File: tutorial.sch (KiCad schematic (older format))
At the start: 129 parts, among them SW0:0 CTRL, SW0:1 SUPER, SW0:10 ALT, SW0:11 MENU, SW0:12 SUPER, SW0:13 CTRL, SW0:2 ALT, SW0:7 SPACE, SW1:0 SHIFT, SW1:10 ., SW1:11 ?, SW1:13 SHIFT, SW1:2 Z, SW1:3 X, SW1:4 C, SW1:5 V, SW1:6 B, SW1:7 N, SW1:8 M, SW1:9 ,, SW2:0 CAPS, SW2:1 A, SW2:10 ;, SW2:11 ', SW2:13 ENTER, SW2:2 S, SW2:3 D, SW2:4 F, SW2:5 G, SW2:6 H, SW2:7 J, SW2:8 K, SW2:9 L, SW3:0 TAB, SW3:1 Q, SW3:10 P, SW3:11 {, SW3:12 }, SW3:13 BCKSL, SW3:2 W, SW3:3 E, SW3:4 R, SW3:5 T, SW3:6 Y, SW3:7 U, SW3:8 I, SW3:9 O, SW4:0 TILDE, SW4:1 1, SW4:10 0, SW4:11 -, SW4:12 =, SW4:13 BCKSP, SW4:2 2, SW4:3 3, SW4:4 4, SW4:5 5, SW4:6 6, SW4:7 7, SW4:8 8, SW4:9 9, U1 TEENSY2.0

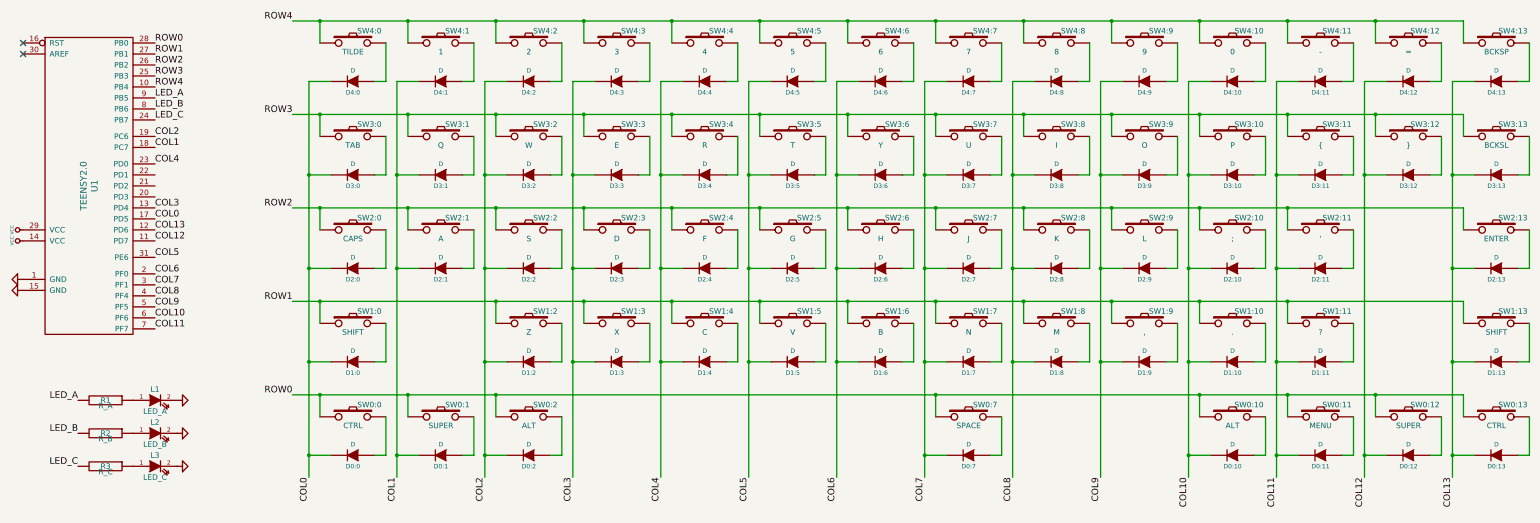
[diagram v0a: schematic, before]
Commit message: Updated to "new" KiCAD formats
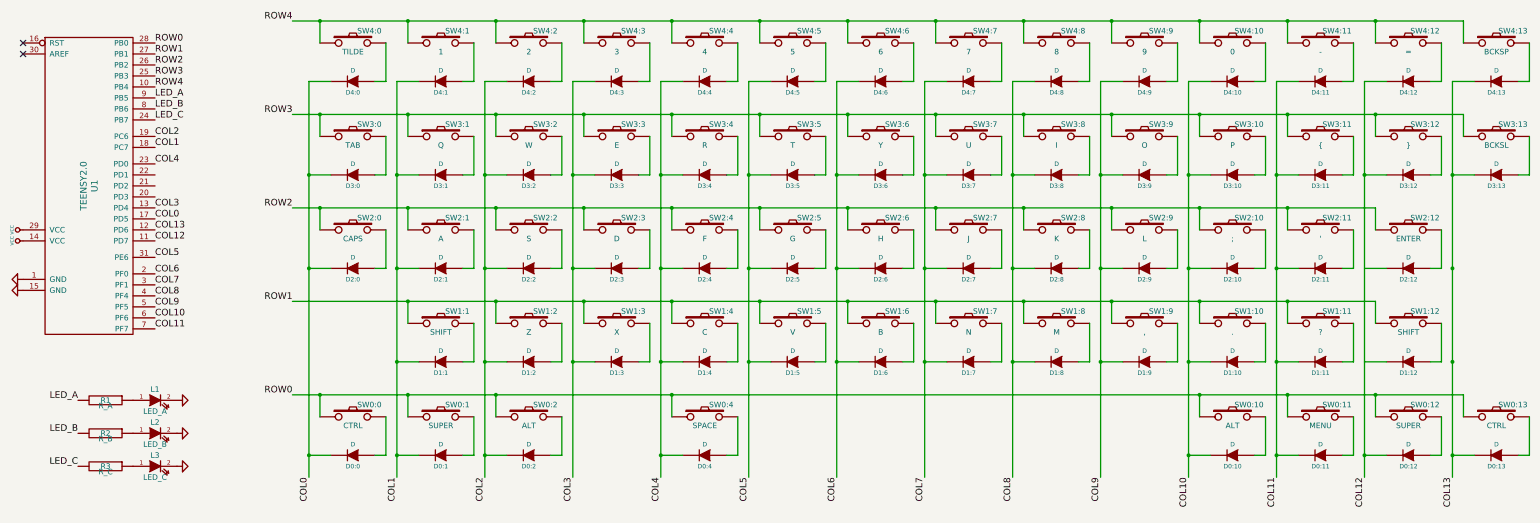
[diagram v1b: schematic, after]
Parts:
- D0:0, D0:1, D0:10, D0:11, D0:12, D0:13, D0:2, D1:10, D1:11, D1:2, D1:3, D1:4, D1:5, D1:6, D1:7, D1:8, D1:9, D2:0, D2:1, D2:10, D2:11, D2:2, D2:3, D2:4, D2:5, D2:6, D2:7, D2:8, D2:9, D3:0, D3:1, D3:10, D3:11, D3:12, D3:13, D3:2, D3:3, D3:4, D3:5, D3:6, D3:7, D3:8, D3:9, D4:0, D4:1, D4:10, D4:11, D4:12, D4:13, D4:2, D4:3, D4:4, D4:5, D4:6, D4:7, D4:8, D4:9: footprint (none) -> footprints:DIODE
- D0:4: renamed from D0:7; footprint (none) -> footprints:DIODE
- D1:1: renamed from D1:0; footprint (none) -> footprints:DIODE
- D1:12: renamed from D1:13; footprint (none) -> footprints:DIODE
- D2:12: renamed from D2:13; footprint (none) -> footprints:DIODE
- L1, L2, L3: footprint (none) -> footprints:CHERRY_MX_LED
- R1, R2, R3: footprint (none) -> footprints:RESISTOR
- SW0:0, SW0:1, SW0:10, SW0:11, SW0:12, SW0:13, SW0:2: footprint (none) -> footprints:CHERRY_PCB_125H
- SW0:4: renamed from SW0:7; footprint (none) -> footprints:CHERRY_PCB_625H
- SW1:1: renamed from SW1:0; footprint (none) -> footprints:CHERRY_PCB_225H
- SW1:10, SW1:11, SW1:2, SW1:3, SW1:4, SW1:5, SW1:6, SW1:7, SW1:8, SW1:9, SW2:1, SW2:10, SW2:11, SW2:2, SW2:3, SW2:4, SW2:5, SW2:6, SW2:7, SW2:8, SW2:9, SW3:1, SW3:10, SW3:11, SW3:12, SW3:2, SW3:3, SW3:4, SW3:5, SW3:6, SW3:7, SW3:8, SW3:9, SW4:0, SW4:1, SW4:10, SW4:11, SW4:12, SW4:2, SW4:3, SW4:4, SW4:5, SW4:6, SW4:7, SW4:8, SW4:9: footprint (none) -> footprints:CHERRY_PCB_100H
- SW1:12: renamed from SW1:13; footprint (none) -> footprints:CHERRY_PCB_275H
- SW2:0: footprint (none) -> footprints:CHERRY_PCB_175H
- SW2:12: renamed from SW2:13; footprint (none) -> footprints:CHERRY_PCB_225H
- SW3:0, SW3:13: footprint (none) -> footprints:CHERRY_PCB_150H
- SW4:13: footprint (none) -> footprints:CHERRY_PCB_200H
- U1: footprint (none) -> footprints:TEENSY_2.0
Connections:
- net COL0: no longer D1:1.2 (K)
- net COL1: now also D1:1.2 (K)
- net COL13: no longer D1:12.2 (K), D2:12.2 (K)
- net COL4: now also D0:4.2 (K)
- net COL7: no longer D0:4.2 (K)
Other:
- moved on the sheet: D0:4, D1:1, D1:12, D2:12, SW0:4, SW1:1, SW1:12, SW2:12
